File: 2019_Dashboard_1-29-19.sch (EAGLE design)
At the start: 55 parts, among them IC1 MCP23017SO, Q1 TN0602N3, Q2 TN0602N3, Q3 TN0602N3, Q4 TN0602N3, Q5 TN0602N3, U1 TLC59281, Y1 16MHz

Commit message: Add files via upload
Finished?
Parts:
- added C10: 100pF, SparkFun-Capacitors:100PF-0603-50V-5%
- added C11: 1.0uF, SparkFun-Capacitors:1.0UF-0805-25V-(+80/-20%)
- added C7: 10uF, SparkFun-Capacitors:10UF-0805-10V-10%
- added C8: 10nF, SparkFun-Capacitors:10NF-0603-50V-10%
- added C9: 22uF, SparkFun-Capacitors:22UF-0805-6.3V-20%
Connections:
- net GND: now also C10.2, C11.2, C7.2, C8.2, C9.2
- net VCC: now also C10.1, C11.1, C7.1, C8.1, C9.1
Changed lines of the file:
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@@
 <part name="SUPPLY8" library="SparkFun-PowerSymbols" library_urn="urn:adsk.eagle:library:530" deviceset="VCC" device=""/>
 <part name="GND1" library="SparkFun-PowerSymbols" library_urn="urn:adsk.eagle:library:530" deviceset="GND" device=""/>
+<part name="C7" library="SparkFun-Capacitors" library_urn="urn:adsk.eagle:library:510" deviceset="10UF" device="-0805-10V-10%" package3d_urn="urn:adsk.eagle:package:37429/1" value="10uF"/>
+<part name="C8" library="SparkFun-Capacitors" library_urn="urn:adsk.eagle:library:510" deviceset="10NF" device="-0603-50V-10%" package3d_urn="urn:adsk.eagle:package:37414/1" value="10nF"/>
+<part name="C9" library="SparkFun-Capacitors" library_urn="urn:adsk.eagle:library:510" deviceset="22UF" device="-0805-6.3V-20%" package3d_urn="urn:adsk.eagle:package:37429/1" value="22uF"/>
+<part name="C10" library="SparkFun-Capacitors" library_urn="urn:adsk.eagle:library:510" deviceset="100PF" device="-0603-50V-5%" package3d_urn="urn:adsk.eagle:package:37414/1" value="100pF"/>
+<part name="C11" library="SparkFun-Capacitors" library_urn="urn:adsk.eagle:library:510" deviceset="1.0UF" device="-0805-25V-(+80/-20%)" package3d_urn="urn:adsk.eagle:package:37429/1" value="1.0uF"/>
 </parts>
 <sheets>
@@
 <instance part="SUPPLY8" gate="G$1" x="-33.02" y="27.94"/>
 <instance part="GND1" gate="1" x="76.2" y="-27.94"/>
+<instance part="C7" gate="G$1" x="-256.54" y="101.6"/>
+<instance part="C8" gate="G$1" x="-238.76" y="101.6"/>
+<instance part="C9" gate="G$1" x="-220.98" y="101.6"/>
+<instance part="C10" gate="G$1" x="-203.2" y="101.6"/>
+<instance part="C11" gate="G$1" x="-276.86" y="101.6"/>
 </instances>
 <busses>
@@
 <wire x1="76.2" y1="5.08" x2="76.2" y2="-10.16" width="0.1524" layer="91"/>
 <junction x="76.2" y="-10.16"/>
+</segment>
+<segment>
+<pinref part="C10" gate="G$1" pin="2"/>
+<wire x1="-203.2" y1="99.06" x2="-203.2" y2="91.44" width="0.1524" layer="91"/>
+<label x="-200.66" y="91.44" size="1.778" layer="95"/>
+</segment>
+<segment>
+<pinref part="C9" gate="G$1" pin="2"/>
+<wire x1="-220.98" y1="99.06" x2="-220.98" y2="91.44" width="0.1524" layer="91"/>
+<label x="-218.44" y="91.44" size="1.778" layer="95"/>
+</segment>
+<segment>
+<pinref part="C8" gate="G$1" pin="2"/>
+<wire x1="-238.76" y1="99.06" x2="-238.76" y2="91.44" width="0.1524" layer="91"/>
+<label x="-236.22" y="91.44" size="1.778" layer="95"/>
+</segment>
+<segment>
+<pinref part="C7" gate="G$1" pin="2"/>
+<wire x1="-256.54" y1="99.06" x2="-256.54" y2="91.44" width="0.1524" layer="91"/>
+<label x="-254" y="91.44" size="1.778" layer="95"/>
+</segment>
+<segment>
+<pinref part="C11" gate="G$1" pin="2"/>
+<wire x1="-276.86" y1="99.06" x2="-276.86" y2="91.44" width="0.1524" layer="91"/>
+<label x="-274.32" y="91.44" size="1.778" layer="95"/>
 </segment>
 </net>
@@
 <wire x1="60.96" y1="12.7" x2="55.88" y2="12.7" width="0.1524" layer="91"/>
 </segment>
-</net>
+<segment>
+<pinref part="C7" gate="G$1" pin="1"/>
+<wire x1="-256.54" y1="106.68" x2="-256.54" y2="111.76" width="0.1524" layer="91"/>
+<label x="-254" y="114.3" size="1.778" layer="95"/>
+</segment>
+<segment>
+<pinref part="C11" gate="G$1" pin="1"/>
+<wire x1="-276.86" y1="106.68" x2="-276.86" y2="111.76" width="0.1524" layer="91"/>
+<label x="-271.78" y="111.76" size="1.778" layer="95"/>
+</segment>
+<segment>
+<pinref part="C8" gate="G$1" pin="1"/>
+<wire x1="-238.76" y1="106.68" x2="-238.76" y2="111.76" width="0.1524" layer="91"/>
+<label x="-236.22" y="111.76" size="1.778" layer="95"/>
+</segment>
+<segment>
+<pinref part="C9" gate="G$1" pin="1"/>
+<wire x1="-220.98" y1="106.68" x2="-220.98" y2="111.76" width="0.1524" layer="91"/>
+<label x="-218.44" y="111.76" size="1.778" layer="95"/>
+</segment>
+<segment>
+<pinref part="C10" gate="G$1" pin="1"/>
+<wire x1="-203.2" y1="106.68" x2="-203.2" y2="111.76" width="0.1524" layer="91"/>
+<label x="-200.66" y="111.76" size="1.778" layer="95"/>
+</segment>
+</net>

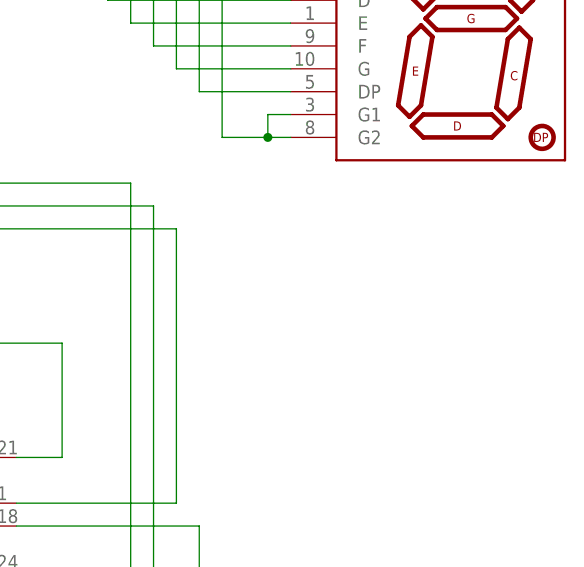
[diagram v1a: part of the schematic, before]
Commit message: Added correct footprint for gear position display
Committing before I actually wire it up
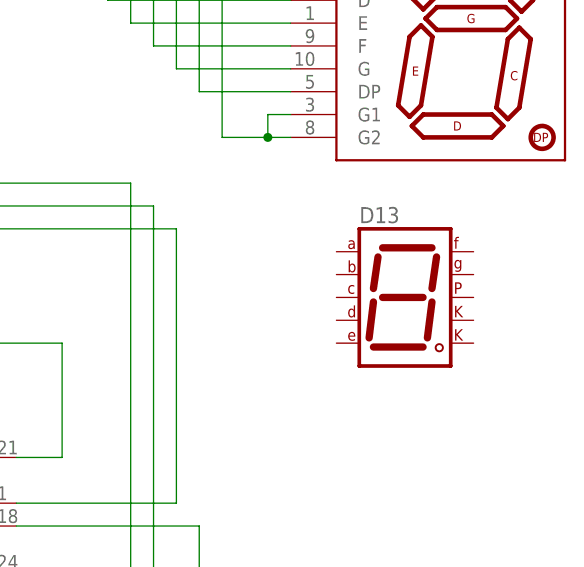
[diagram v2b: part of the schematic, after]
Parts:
- added D13: (no value), special:7SEG-CK
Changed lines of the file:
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@@
 <?xml version="1.0" encoding="utf-8"?>
 <!DOCTYPE eagle SYSTEM "eagle.dtd">
-<eagle version="9.1.3">
+<eagle version="9.1.0">
 <drawing>
 <settings>
@@
 <part name="C10" library="SparkFun-Capacitors" library_urn="urn:adsk.eagle:library:510" deviceset="100PF" device="-0603-50V-5%" package3d_urn="urn:adsk.eagle:package:37414/1" value="100pF"/>
 <part name="C11" library="SparkFun-Capacitors" library_urn="urn:adsk.eagle:library:510" deviceset="1.0UF" device="-0805-25V-(+80/-20%)" package3d_urn="urn:adsk.eagle:package:37429/1" value="1.0uF"/>
+<part name="D13" library="special" library_urn="urn:adsk.eagle:library:367" deviceset="7SEG-CK" device="" package3d_urn="urn:adsk.eagle:package:26668/2"/>
 </parts>
 <sheets>
@@
 <instance part="C10" gate="G$1" x="-203.2" y="101.6"/>
 <instance part="C11" gate="G$1" x="-276.86" y="101.6"/>
+<instance part="D13" gate="G$1" x="99.06" y="30.48"/>
 </instances>
 <busses>
